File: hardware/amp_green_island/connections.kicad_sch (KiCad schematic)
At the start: 5 parts, among them J501 input, J502 output, J503 Conn_01x04_Pin

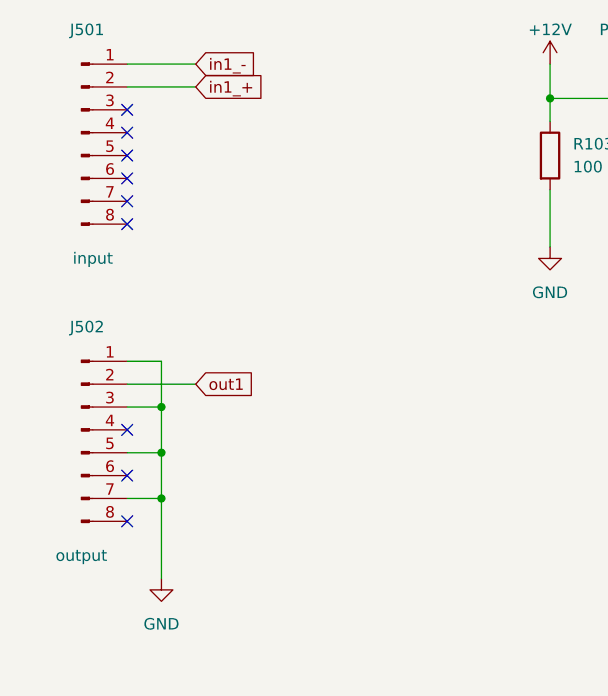
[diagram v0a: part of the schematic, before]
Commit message: amp_green_island: add all 4 channels to schematic
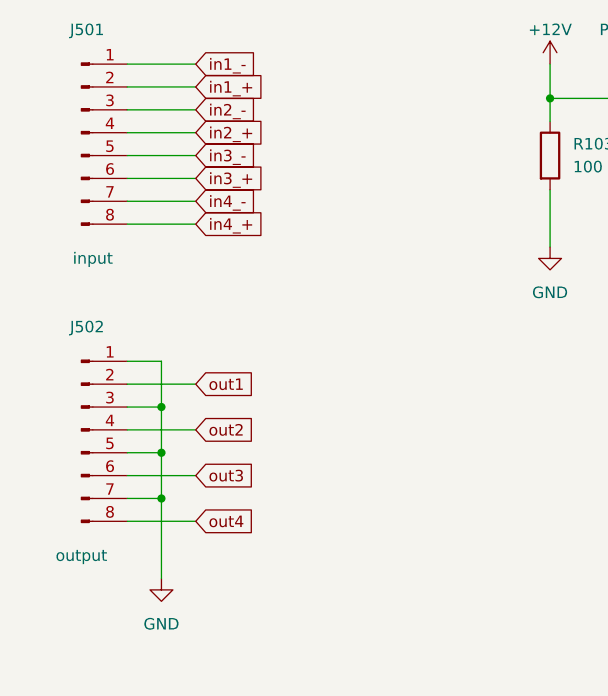
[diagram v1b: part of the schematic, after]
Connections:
- net in2_-: now reaches J501.3 (Pin_3)
- net in2_+: now reaches J501.4 (Pin_4)
- net in3_-: now reaches J501.5 (Pin_5)
- net in3_+: now reaches J501.6 (Pin_6)
- net in4_-: now reaches J501.7 (Pin_7)
- net in4_+: now reaches J501.8 (Pin_8)
- net out2: now reaches J502.4 (Pin_4)
- net out3: now reaches J502.6 (Pin_6)
- net out4: now reaches J502.8 (Pin_8)
- no-connect marks 9 -> 0
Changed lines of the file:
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@@
   (junction (at 201.93 74.93) (diameter 0) (color 0 0 0 0)
   )
-  (no_connect (at 124.46 81.28))
-  (no_connect (at 124.46 88.9))
-  (no_connect (at 124.46 111.76))
-  (no_connect (at 124.46 83.82))
-  (no_connect (at 124.46 86.36))
-  (no_connect (at 124.46 116.84))
-  (no_connect (at 124.46 121.92))
-  (no_connect (at 124.46 78.74))
-  (no_connect (at 124.46 76.2))
   (wire (pts (xy 128.27 109.22) (xy 128.27 114.3))
     (stroke (width 0) (type default))
   )
+  (wire (pts (xy 124.46 83.82) (xy 132.08 83.82))
+    (stroke (width 0) (type default))
+  )
   (wire (pts (xy 125.73 153.67) (xy 144.78 153.67))
+    (stroke (width 0) (type default))
+  )
+  (wire (pts (xy 124.46 88.9) (xy 132.08 88.9))
     (stroke (width 0) (type default))
   )
@@
   )
   (wire (pts (xy 212.09 71.12) (xy 212.09 74.93))
+    (stroke (width 0) (type default))
+  )
+  (wire (pts (xy 124.46 86.36) (xy 132.08 86.36))
     (stroke (width 0) (type default))
   )
@@
   )
   (wire (pts (xy 181.61 71.12) (xy 181.61 74.93))
+    (stroke (width 0) (type default))
+  )
+  (wire (pts (xy 124.46 116.84) (xy 132.08 116.84))
+    (stroke (width 0) (type default))
+  )
+  (wire (pts (xy 124.46 78.74) (xy 132.08 78.74))
     (stroke (width 0) (type default))
   )
@@
     (stroke (width 0) (type default))
   )
+  (wire (pts (xy 124.46 81.28) (xy 132.08 81.28))
+    (stroke (width 0) (type default))
+  )
   (wire (pts (xy 124.46 104.14) (xy 128.27 104.14))
     (stroke (width 0) (type default))
@@
   )
   (wire (pts (xy 124.46 119.38) (xy 128.27 119.38))
+    (stroke (width 0) (type default))
+  )
+  (wire (pts (xy 124.46 76.2) (xy 132.08 76.2))
     (stroke (width 0) (type default))
   )
@@
     (stroke (width 0) (type default))
   )
+  (wire (pts (xy 124.46 121.92) (xy 132.08 121.92))
+    (stroke (width 0) (type default))
+  )
   (wire (pts (xy 201.93 87.63) (xy 201.93 91.44))
     (stroke (width 0) (type default))
@@
     (stroke (width 0) (type default))
   )
+  (wire (pts (xy 124.46 111.76) (xy 132.08 111.76))
+    (stroke (width 0) (type default))
+  )
   (global_label "in1_+" (shape input) (at 132.08 73.66 0) (fields_autoplaced)
     (effects (font (size 1.27 1.27)) (justify left))
     (property "Intersheetrefs" "${INTERSHEET_REFS}" (at 140.4891 73.66 0)
+      (effects (font (size 1.27 1.27)) (justify left) hide)
+    )
+  )
+  (global_label "out3" (shape input) (at 132.08 116.84 0) (fields_autoplaced)
+    (effects (font (size 1.27 1.27)) (justify left))
+    (property "Intersheetrefs" "${INTERSHEET_REFS}" (at 139.219 116.84 0)
+      (effects (font (size 1.27 1.27)) (justify left) hide)
+    )
+  )
+  (global_label "in3_+" (shape input) (at 132.08 83.82 0) (fields_autoplaced)
+    (effects (font (size 1.27 1.27)) (justify left))
+    (property "Intersheetrefs" "${INTERSHEET_REFS}" (at 140.4891 83.82 0)
+      (effects (font (size 1.27 1.27)) (justify left) hide)
+    )
+  )
+  (global_label "in4_+" (shape input) (at 132.08 88.9 0) (fields_autoplaced)
+    (effects (font (size 1.27 1.27)) (justify left))
+    (property "Intersheetrefs" "${INTERSHEET_REFS}" (at 140.4891 88.9 0)
+      (effects (font (size 1.27 1.27)) (justify left) hide)
+    )
+  )
+  (global_label "in4_-" (shape input) (at 132.08 86.36 0) (fields_autoplaced)
+    (effects (font (size 1.27 1.27)) (justify left))
+    (property "Intersheetrefs" "${INTERSHEET_REFS}" (at 140.4891 86.36 0)
+      (effects (font (size 1.27 1.27)) (justify left) hide)
+    )
+  )
+  (global_label "out4" (shape input) (at 132.08 121.92 0) (fields_autoplaced)
+    (effects (font (size 1.27 1.27)) (justify left))
+    (property "Intersheetrefs" "${INTERSHEET_REFS}" (at 139.219 121.92 0)
+      (effects (font (size 1.27 1.27)) (justify left) hide)
+    )
+  )
+  (global_label "out2" (shape input) (at 132.08 111.76 0) (fields_autoplaced)
+    (effects (font (size 1.27 1.27)) (justify left))
+    (property "Intersheetrefs" "${INTERSHEET_REFS}" (at 139.219 111.76 0)
+      (effects (font (size 1.27 1.27)) (justify left) hide)
+    )
+  )
+  (global_label "in2_-" (shape input) (at 132.08 76.2 0) (fields_autoplaced)
+    (effects (font (size 1.27 1.27)) (justify left))
+    (property "Intersheetrefs" "${INTERSHEET_REFS}" (at 140.4891 76.2 0)
       (effects (font (size 1.27 1.27)) (justify left) hide)
     )
@@
     )
   )
+  (global_label "in2_+" (shape input) (at 132.08 78.74 0) (fields_autoplaced)
+    (effects (font (size 1.27 1.27)) (justify left))
+    (property "Intersheetrefs" "${INTERSHEET_REFS}" (at 140.4891 78.74 0)
+      (effects (font (size 1.27 1.27)) (justify left) hide)
+    )
+  )
   (global_label "out1" (shape input) (at 132.08 106.68 0) (fields_autoplaced)
     (effects (font (size 1.27 1.27)) (justify left))
@@
       (effects (font (size 1.27 1.27)) (justify left) hide)
     )
+  )
+  (global_label "in3_-" (shape input) (at 132.08 81.28 0) (fields_autoplaced)
+    (effects (font (size 1.27 1.27)) (justify left))
+    (property "Intersheetrefs" "${INTERSHEET_REFS}" (at 140.4891 81.28 0)
+      (effects (font (size 1.27 1.27)) (justify left) hide)
+    )

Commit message: green_island: pcb routing done
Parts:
- added C501, C502: 220u, Capacitor_SMD:C_Elec_8x10.2, symbol Device:C_Polarized
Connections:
- net +12V: now also C501.1
- net -12V: now also C502.2
- net GND: now also J502.2 (Pin_2), J502.4 (Pin_4), J502.6 (Pin_6), J502.8 (Pin_8), C501.2, C502.1; no longer J502.1 (Pin_1), J502.3 (Pin_3), J502.5 (Pin_5), J502.7 (Pin_7)
- net out1: now also J502.1 (Pin_1); no longer J502.2 (Pin_2)
- net out2: now also J502.3 (Pin_3); no longer J502.4 (Pin_4)
- net out3: now also J502.5 (Pin_5); no longer J502.6 (Pin_6)
- net out4: now also J502.7 (Pin_7); no longer J502.8 (Pin_8)
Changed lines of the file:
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@@
 (kicad_sch (version 20230121) (generator eeschema)
   (paper "A4")
-  (junction (at 128.27 119.38) (diameter 0) (color 0 0 0 0)
+  (junction (at 128.27 111.76) (diameter 0) (color 0 0 0 0)
+  )
+  (junction (at 128.27 121.92) (diameter 0) (color 0 0 0 0)
+  )
+  (junction (at 212.09 87.63) (diameter 0) (color 0 0 0 0)
+  )
+  (junction (at 128.27 116.84) (diameter 0) (color 0 0 0 0)
+  )
+  (junction (at 171.45 87.63) (diameter 0) (color 0 0 0 0)
   )
   (junction (at 201.93 87.63) (diameter 0) (color 0 0 0 0)
   )
-  (junction (at 128.27 109.22) (diameter 0) (color 0 0 0 0)
+  (junction (at 181.61 74.93) (diameter 0) (color 0 0 0 0)
+  )
+  (junction (at 212.09 74.93) (diameter 0) (color 0 0 0 0)
   )
   (junction (at 171.45 74.93) (diameter 0) (color 0 0 0 0)
@@
   (junction (at 129.54 156.21) (diameter 0) (color 0 0 0 0)
   )
-  (junction (at 128.27 114.3) (diameter 0) (color 0 0 0 0)
-  )
   (junction (at 201.93 74.93) (diameter 0) (color 0 0 0 0)
   )
-  (wire (pts (xy 128.27 109.22) (xy 128.27 114.3))
-    (stroke (width 0) (type default))
-  )
   (wire (pts (xy 124.46 83.82) (xy 132.08 83.82))
     (stroke (width 0) (type default))
   )
+  (wire (pts (xy 124.46 111.76) (xy 128.27 111.76))
+    (stroke (width 0) (type default))
+  )
   (wire (pts (xy 125.73 153.67) (xy 144.78 153.67))
     (stroke (width 0) (type default))
@@
     (stroke (width 0) (type default))
   )
+  (wire (pts (xy 124.46 116.84) (xy 128.27 116.84))
+    (stroke (width 0) (type default))
+  )
+  (wire (pts (xy 128.27 106.68) (xy 128.27 111.76))
+    (stroke (width 0) (type default))
+  )
   (wire (pts (xy 171.45 71.12) (xy 171.45 74.93))
     (stroke (width 0) (type default))
@@
     (stroke (width 0) (type default))
   )
+  (wire (pts (xy 212.09 74.93) (xy 212.09 77.47))
+    (stroke (width 0) (type default))
+  )
   (wire (pts (xy 212.09 71.12) (xy 212.09 74.93))
     (stroke (width 0) (type default))
@@
     (stroke (width 0) (type default))
   )
-  (wire (pts (xy 171.45 85.09) (xy 171.45 91.44))
-    (stroke (width 0) (type default))
-  )
-  (wire (pts (xy 124.46 106.68) (xy 132.08 106.68))
-    (stroke (width 0) (type default))
-  )
-  (wire (pts (xy 124.46 109.22) (xy 128.27 109.22))
-    (stroke (width 0) (type default))
-  )
-  (wire (pts (xy 128.27 104.14) (xy 128.27 109.22))
+  (wire (pts (xy 171.45 85.09) (xy 171.45 87.63))
+    (stroke (width 0) (type default))
+  )
+  (wire (pts (xy 124.46 106.68) (xy 128.27 106.68))
+    (stroke (width 0) (type default))
+  )
+  (wire (pts (xy 181.61 87.63) (xy 181.61 85.09))
+    (stroke (width 0) (type default))
+  )
+  (wire (pts (xy 124.46 104.14) (xy 132.08 104.14))
     (stroke (width 0) (type default))
   )
@@
     (stroke (width 0) (type default))
   )
-  (wire (pts (xy 124.46 116.84) (xy 132.08 116.84))
+  (wire (pts (xy 128.27 116.84) (xy 128.27 121.92))
     (stroke (width 0) (type default))
   )
@@
     (stroke (width 0) (type default))
   )
+  (wire (pts (xy 171.45 87.63) (xy 181.61 87.63))
+    (stroke (width 0) (type default))
+  )
+  (wire (pts (xy 128.27 121.92) (xy 128.27 128.27))
+    (stroke (width 0) (type default))
+  )
   (wire (pts (xy 125.73 148.59) (xy 134.62 148.59))
     (stroke (width 0) (type default))
@@
     (stroke (width 0) (type default))
   )
-  (wire (pts (xy 128.27 119.38) (xy 128.27 128.27))
-    (stroke (width 0) (type default))
-  )
   (wire (pts (xy 201.93 87.63) (xy 212.09 87.63))
     (stroke (width 0) (type default))
@@
     (stroke (width 0) (type default))
   )
+  (wire (pts (xy 124.46 121.92) (xy 128.27 121.92))
+    (stroke (width 0) (type default))
+  )
   (wire (pts (xy 124.46 81.28) (xy 132.08 81.28))
     (stroke (width 0) (type default))
   )
-  (wire (pts (xy 124.46 104.14) (xy 128.27 104.14))
-    (stroke (width 0) (type default))
-  )
   (wire (pts (xy 201.93 74.93) (xy 201.93 77.47))
     (stroke (width 0) (type default))
   )
-  (wire (pts (xy 124.46 119.38) (xy 128.27 119.38))
+  (wire (pts (xy 171.45 87.63) (xy 171.45 91.44))
     (stroke (width 0) (type default))
   )
@@
     (stroke (width 0) (type default))
   )
-  (wire (pts (xy 124.46 114.3) (xy 128.27 114.3))
-    (stroke (width 0) (type default))
-  )
   (wire (pts (xy 129.54 151.13) (xy 129.54 156.21))
     (stroke (width 0) (type default))
@@
     (stroke (width 0) (type default))
   )
-  (wire (pts (xy 128.27 114.3) (xy 128.27 119.38))
+  (wire (pts (xy 124.46 114.3) (xy 132.08 114.3))
     (stroke (width 0) (type default))
   )
@@
     (stroke (width 0) (type default))
   )
-  (wire (pts (xy 124.46 121.92) (xy 132.08 121.92))
+  (wire (pts (xy 212.09 85.09) (xy 212.09 87.63))
+    (stroke (width 0) (type default))
+  )
+  (wire (pts (xy 124.46 119.38) (xy 132.08 119.38))
     (stroke (width 0) (type default))
   )
@@
     (stroke (width 0) (type default))
   )
-  (wire (pts (xy 124.46 111.76) (xy 132.08 111.76))
+  (wire (pts (xy 128.27 111.76) (xy 128.27 116.84))
+    (stroke (width 0) (type default))
+  )
+  (wire (pts (xy 124.46 109.22) (xy 132.08 109.22))
+    (stroke (width 0) (type default))
+  )
+  (wire (pts (xy 181.61 74.93) (xy 181.61 77.47))
     (stroke (width 0) (type default))
   )
@@
     )
   )
-  (global_label "out3" (shape input) (at 132.08 116.84 0) (fields_autoplaced)
-    (effects (font (size 1.27 1.27)) (justify left))
-    (property "Intersheetrefs" "${INTERSHEET_REFS}" (at 139.219 116.84 0)
+  (global_label "out3" (shape input) (at 132.08 114.3 0) (fields_autoplaced)
+    (effects (font (size 1.27 1.27)) (justify left))
+    (property "Intersheetrefs" "${INTERSHEET_REFS}" (at 139.219 114.3 0)
       (effects (font (size 1.27 1.27)) (justify left) hide)
     )
@@
     )
   )
-  (global_label "out4" (shape input) (at 132.08 121.92 0) (fields_autoplaced)
-    (effects (font (size 1.27 1.27)) (justify left))
-    (property "Intersheetrefs" "${INTERSHEET_REFS}" (at 139.219 121.92 0)
-      (effects (font (size 1.27 1.27)) (justify left) hide)
-    )
-  )
-  (global_label "out2" (shape input) (at 132.08 111.76 0) (fields_autoplaced)
-    (effects (font (size 1.27 1.27)) (justify left))
-    (property "Intersheetrefs" "${INTERSHEET_REFS}" (at 139.219 111.76 0)
+  (global_label "out4" (shape input) (at 132.08 119.38 0) (fields_autoplaced)
+    (effects (font (size 1.27 1.27)) (justify left))
+    (property "Intersheetrefs" "${INTERSHEET_REFS}" (at 139.219 119.38 0)
+      (effects (font (size 1.27 1.27)) (justify left) hide)
+    )
+  )
+  (global_label "out2" (shape input) (at 132.08 109.22 0) (fields_autoplaced)
+    (effects (font (size 1.27 1.27)) (justify left))
+    (property "Intersheetrefs" "${INTERSHEET_REFS}" (at 139.219 109.22 0)
       (effects (font (size 1.27 1.27)) (justify left) hide)
     )
@@
     )
   )
-  (global_label "out1" (shape input) (at 132.08 106.68 0) (fields_autoplaced)
-    (effects (font (size 1.27 1.27)) (justify left))
-    (property "Intersheetrefs" "${INTERSHEET_REFS}" (at 139.219 106.68 0)
+  (global_label "out1" (shape input) (at 132.08 104.14 0) (fields_autoplaced)
+    (effects (font (size 1.27 1.27)) (justify left))
+    (property "Intersheetrefs" "${INTERSHEET_REFS}" (at 139.219 104.14 0)
       (effects (font (size 1.27 1.27)) (justify left) hide)
     )
@@
     (property "Intersheetrefs" "${INTERSHEET_REFS}" (at 140.4891 81.28 0)
       (effects (font (size 1.27 1.27)) (justify left) hide)
+    )
+  )
+  (symbol (lib_id "Device:C_Polarized") (at 212.09 81.28 180) (unit 1)
+    (in_bom yes) (on_board yes) (dnp no)
+    (property "Reference" "C502" (at 215.9 80.01 0)
+      (effects (font (size 1.27 1.27)) (justify right))
+    )
+    (property "Value" "220u" (at 215.9 82.55 0)
+      (effects (font (size 1.27 1.27)) (justify right))
+    )
+    (property "Footprint" "Capacitor_SMD:C_Elec_8x10.2" (at 211.1248 77.47 0)
+      (effects (font (size 1.27 1.27)) hide)
+    )
+    (property "Datasheet" "~" (at 212.09 81.28 0)
+      (effects (font (size 1.27 1.27)) hide)
+    )
+    (pin "1")
+    (pin "2")
+    (instances
+      (project "amp_green_island"
+        (path "/43b74afa-5a12-461c-abea-555792070363/0e182138-df54-4e11-b7e0-1289ccbdc8e5"
+          (reference "C502") (unit 1)
+        )
+      )
     )
   )
@@
         )
       )
+    )
+  )
+  (symbol (lib_id "Device:C_Polarized") (at 181.61 81.28 0) (unit 1)
+    (in_bom yes) (on_board yes) (dnp no)
+    (property "Reference" "C501" (at 189.23 80.01 0)
+      (effects (font (size 1.27 1.27)) (justify right))
+    )
+    (property "Value" "220u" (at 189.23 82.55 0)
+      (effects (font (size 1.27 1.27)) (justify right))
+    )
+    (property "Footprint" "Capacitor_SMD:C_Elec_8x10.2" (at 182.5752 85.09 0)
+      (effects (font (size 1.27 1.27)) hide)
+    )
+    (property "Datasheet" "~" (at 181.61 81.28 0)
+      (effects (font (size 1.27 1.27)) hide)
+    )
+    (pin "1")
+    (pin "2")
+    (instances
+      (project "amp_green_island"
+        (path "/43b74afa-5a12-461c-abea-555792070363/0e182138-df54-4e11-b7e0-1289ccbdc8e5"
+          (reference "C501") (unit 1)
+        )
+      )

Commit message: amp_green_island: pcb verified
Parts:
- added D501, D502: LED, LED_SMD:LED_0805_2012Metric_Pad1.15x1.40mm_HandSolder, symbol Device:LED
- added R105 (x2): 100k, Resistor_SMD:R_0805_2012Metric_Pad1.20x1.40mm_HandSolder, symbol Device:R
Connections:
- net +12V: now also R105.1
- net -12V: now also R105.1
- net GND: now also D501.1 (K), D502.2 (A)
- new net: D502.1 (K), R105.2
- new net: D501.2 (A), R105.2
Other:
- moved on the sheet: C502, R108
